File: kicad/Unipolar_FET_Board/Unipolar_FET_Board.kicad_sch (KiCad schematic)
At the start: 20 parts, among them J1 Screw_Terminal_01x04, J3 SENSE, J4 N-MOS, Q1 Q_NMOS_GDS, Q2 Q_NMOS_GDS

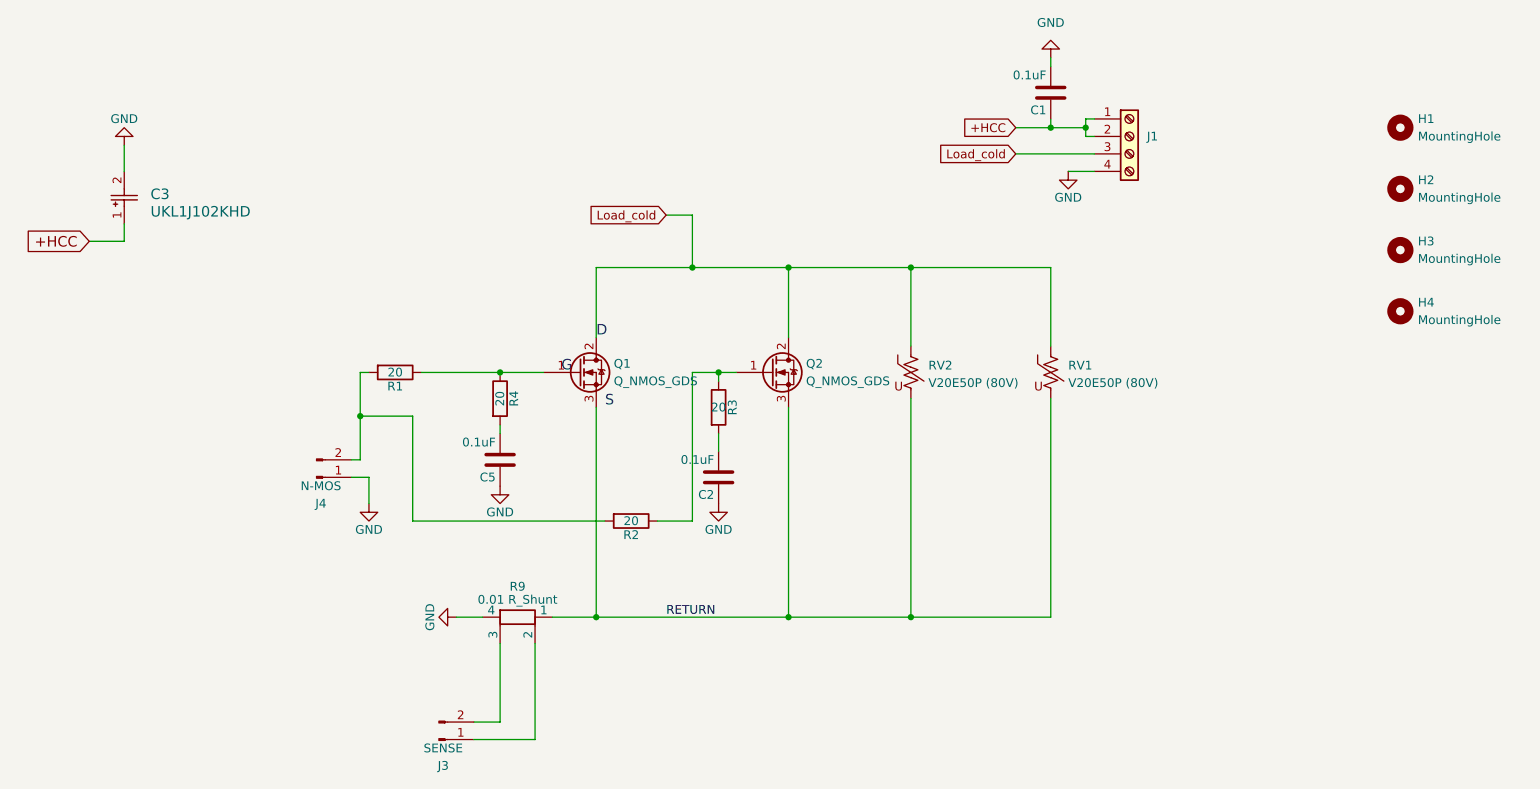
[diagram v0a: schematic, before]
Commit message: Final Board schematics and layouts, Also added custom footprints that were made for the relay and terminal connector block.
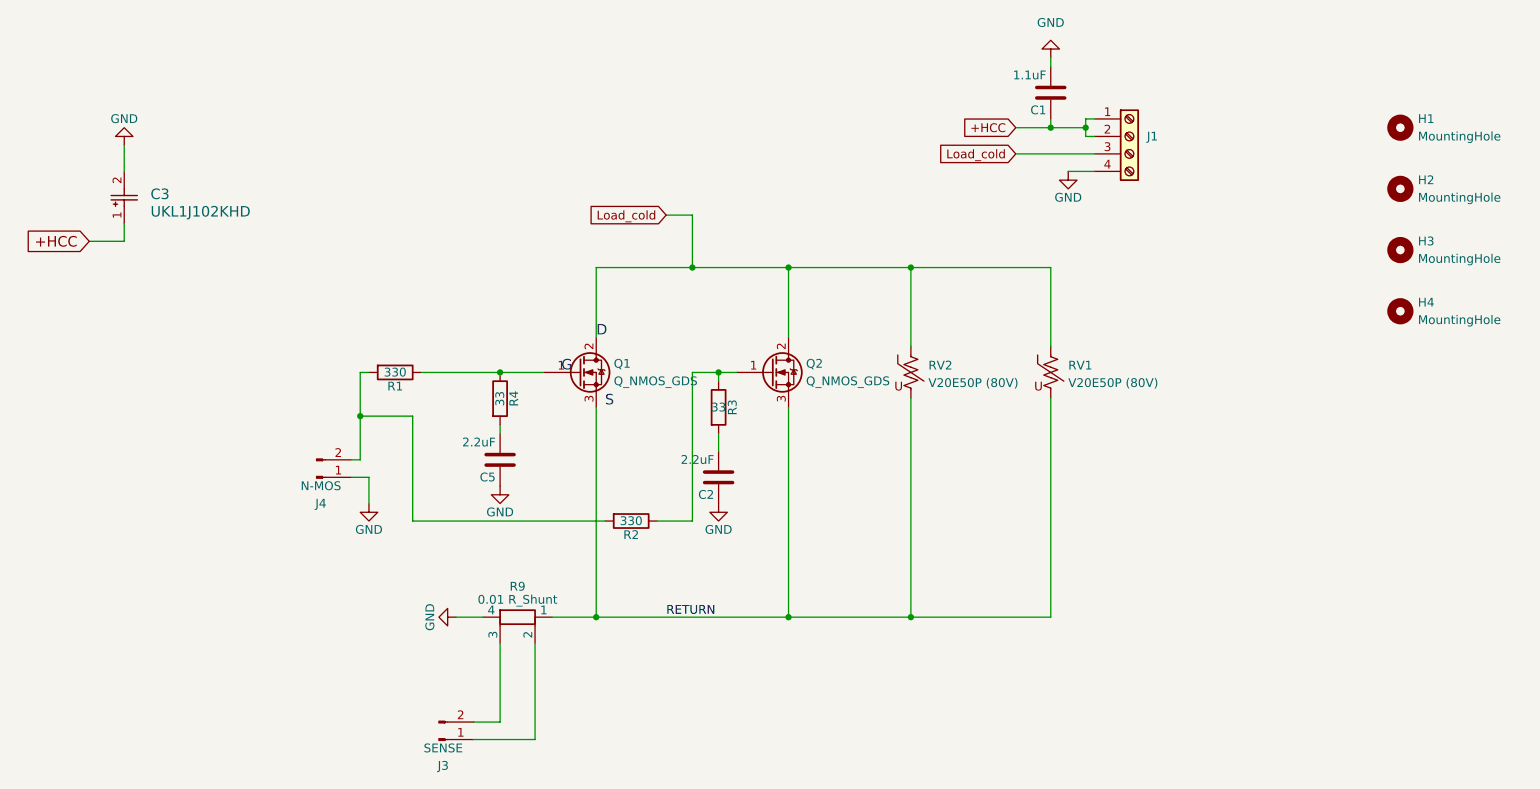
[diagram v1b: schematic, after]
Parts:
- C1: value 0.1uF -> 1.1uF
- C2, C5: value 0.1uF -> 2.2uF
- R1, R2: value 20 -> 330
- R3, R4: value 20 -> 33
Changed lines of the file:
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@@
 			)
 		)
-		(property "Value" "0.1uF"
+		(property "Value" "2.2uF"
 			(at 120.015 78.74 0)
 			(effects
@@
 			)
 		)
-		(property "Value" "20"
+		(property "Value" "330"
 			(at 105.41 68.58 90)
 			(effects
@@
 			)
 		)
-		(property "Value" "20"
+		(property "Value" "330"
 			(at 139.7 90.17 90)
 			(effects
@@
 			)
 		)
-		(property "Value" "0.1uF"
+		(property "Value" "2.2uF"
 			(at 151.765 81.28 0)
 			(effects
@@
 			)
 		)
-		(property "Value" "20"
+		(property "Value" "33"
 			(at 120.65 72.39 90)
 			(effects
@@
 			)
 		)
-		(property "Value" "20"
+		(property "Value" "33"
 			(at 152.4 73.66 0)
 			(effects
@@
 			)
 		)
-		(property "Value" "0.1uF"
+		(property "Value" "1.1uF"
 			(at 200.025 25.4 0)
 			(effects
